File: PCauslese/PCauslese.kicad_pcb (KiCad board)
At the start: 2 copper layers, 78.7 x 24.1 mm, 29 parts, among them J1 Bally/Bergmann, J2 VDAI, J3 ADP alt, J4 ESP-01, J5 FT232, J7 USB TO TTL, J8 CP2102, U1 ULN2003A, U2 AMS1117-3.3, U4 MAX3232

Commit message: nochmal
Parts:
- added C8: C_Polarized, Capacitor_Tantalum_SMD:CP_EIA-3528-15_AVX-H, F.Cu at (119.7, 65.4)
- added C9: C_Polarized, Capacitor_Tantalum_SMD:CP_EIA-3528-15_AVX-H, F.Cu at (119.7, 69.2)
- added J6: Conn_01x08, Connector_PinHeader_2.54mm:PinHeader_1x08_P2.54mm_Vertical, F.Cu at (103.5, 66.0)
- added J9: Conn_01x08, Connector_PinHeader_2.54mm:PinHeader_1x08_P2.54mm_Vertical, F.Cu at (106.0, 66.0)
- added U3: AMS1117-5.0, Package_TO_SOT_SMD:SOT-223-3_TabPin2, F.Cu at (112.4, 69.0)
- moved J7 115.9 mm to (218.4, 46.4), turned to 0 degrees
- moved C7 109.4 mm to (194.9, 60.2)
- moved C1 105.7 mm to (178.4, 34.0), turned to 0 degrees
- moved J8 101.5 mm to (214.0, 43.2), turned to 0 degrees
- moved J5 100.0 mm to (209.4, 43.2), turned to 0 degrees
- moved U2 94.6 mm to (174.7, 22.2), turned to 0 degrees
- moved D1 92.9 mm to (206.5, 25.7)
- moved J4 92.2 mm to (194.9, 42.5), turned to 0 degrees
- moved R8 85.3 mm to (192.2, 36.2), turned to 0 degrees
- moved C2 85.1 mm to (178.4, 38.4), turned to 0 degrees
- moved C5 85.1 mm to (178.4, 51.4)
- moved C3 82.9 mm to (178.4, 42.7), turned to 0 degrees
- moved R9 82.8 mm to (188.4, 44.5)
- moved C4 79.0 mm to (178.4, 47.1), turned to 0 degrees
- moved U4 75.5 mm to (167.0, 43.8), turned to 0 degrees
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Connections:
- R2 pad 1: +3.3V -> VDDA
- R3 pad 1: +3.3V -> VDDA
- R4 pad 1: +3.3V -> VDDA
- R5 pad 1: +3.3V -> VDDA
- R7 pad 1: +3.3V -> VDDA
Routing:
- net +3.3V: track 86.1 -> 0.00 mm, vias 1 -> 0
- net GND: track 65.5 -> 6.99 mm, vias 13 -> 36
- net +48V: track 0.00 -> 48.3 mm
- net /DTR: track 44.1 -> 0.00 mm, vias 1 -> 0
- net BUSY: track 90.3 -> 48.3 mm, vias 1 -> 0
- net /RX: track 42.0 -> 0.00 mm
- net /TX: track 36.5 -> 0.00 mm
- net TX1: track 82.8 -> 52.7 mm
- net VDDA: track 0.00 -> 27.3 mm
- net Net-(D1-DIN): track 24.9 -> 0.00 mm
- net Net-(U1-I6): track 20.5 -> 0.00 mm
- net Net-(U4-VS+): track 14.6 -> 0.00 mm
- net RX1: track 94.8 -> 80.6 mm, vias 1 -> 0
- net Net-(JP1-A): track 17.2 -> 30.6 mm, vias 1 -> 0
- net Net-(U4-VS-): track 10.6 -> 0.00 mm
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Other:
- board text removed: "48V"
- board text removed: "BUSY"
- board text removed: "DTR"
- board text removed: "GND"
- board text removed: "MAX3232(3V) MAX232 (5V)"
- board text removed: "RX"
- board text removed: "SSA"
- board text removed: "SSE"
- board text removed: "TX"
- board text removed: "VPP"
- board text removed: "normal"

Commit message: max mit esp
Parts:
- added J10: Conn_01x05, Connector_PinHeader_2.54mm:PinHeader_1x05_P2.54mm_Vertical, F.Cu at (129.5, 69.8)
- added J11: Conn_01x05, Connector_PinHeader_2.54mm:PinHeader_1x05_P2.54mm_Vertical, F.Cu at (132.1, 69.8)
- U2: value AMS1117-3.3 -> 1117-3.3
- U3: value AMS1117-5.0 -> 1117-5.0
- moved D1 89.9 mm to (137.7, 83.6), turned to 180 degrees
- moved J7 69.9 mm to (160.7, 85.7), turned to 90 degrees
- moved U2 61.3 mm to (139.5, 72.4), turned to -90 degrees
- moved J8 53.7 mm to (165.7, 66.7)
- moved J5 53.5 mm to (161.3, 66.7)
- moved C1 53.5 mm to (135.5, 66.0), turned to 180 degrees
- moved R8 52.0 mm to (148.8, 64.8)
- moved C7 50.6 mm to (144.6, 66.0), turned to 180 degrees
- moved C3 48.2 mm to (153.7, 84.1), turned to 90 degrees
- moved J4 47.9 mm to (155.6, 69.8), turned to -90 degrees
- moved C2 46.8 mm to (140.7, 66.0)
- moved C6 43.4 mm to (147.1, 85.7), turned to 180 degrees
- moved R9 41.0 mm to (152.8, 64.8)
- moved C4 40.4 mm to (153.7, 79.0), turned to 90 degrees
- moved U4 40.1 mm to (147.4, 78.7), turned to 180 degrees
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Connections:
- C1 pad 1: VPP -> VDDA
- U2 pad 3: VPP -> VDDA
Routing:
- net +3.3V: track 0.00 -> 51.6 mm, vias 0 -> 3
- net /RX: track 0.00 -> 42.4 mm
- net Net-(J10-Pin_3): track 0.00 -> 39.5 mm, vias 0 -> 2
- net /TX: track 0.00 -> 38.8 mm
- net Net-(D1-DIN): track 0.00 -> 36.8 mm, vias 0 -> 1
- net VDDA: track 27.3 -> 62.7 mm, vias 0 -> 1
- net /DTR: track 0.00 -> 34.8 mm
- net Net-(J10-Pin_5): track 0.00 -> 27.7 mm
- net Net-(J10-Pin_1): track 0.00 -> 23.0 mm, vias 0 -> 1
- net GND: track 6.99 -> 12.9 mm, vias 36 -> 75
- net Net-(U4-VS+): track 0.00 -> 5.20 mm
- net Net-(U4-VS-): track 0.00 -> 5.09 mm
- net Net-(U4-C1+): track 0.00 -> 4.82 mm
- net Net-(U4-C1-): track 0.00 -> 4.60 mm
- net Net-(U4-C2+): track 0.00 -> 4.29 mm
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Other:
- board size 78.7 x 24.1 mm -> 97.2 x 24.1 mm
- board text added: "40V"
- board text added: "BUSY"
- board text added: "DTR"
- board text added: "GND"
- board text added: "JLCJLCJLCJLC"
- board text added: "RX"
- board text added: "RX1"
- board text added: "RX2"
- board text added: "Stecker"
- board text added: "TX"
- board text added: "TX1"
- board text added: "TX2"
- board text added: "VDD"
- board text added: "VPP"
- board text added: "Verstärker /Adapter"
- board text added: "https://github.com/stonedDiscord/Automatenplatinen"
- board text added: "normal"

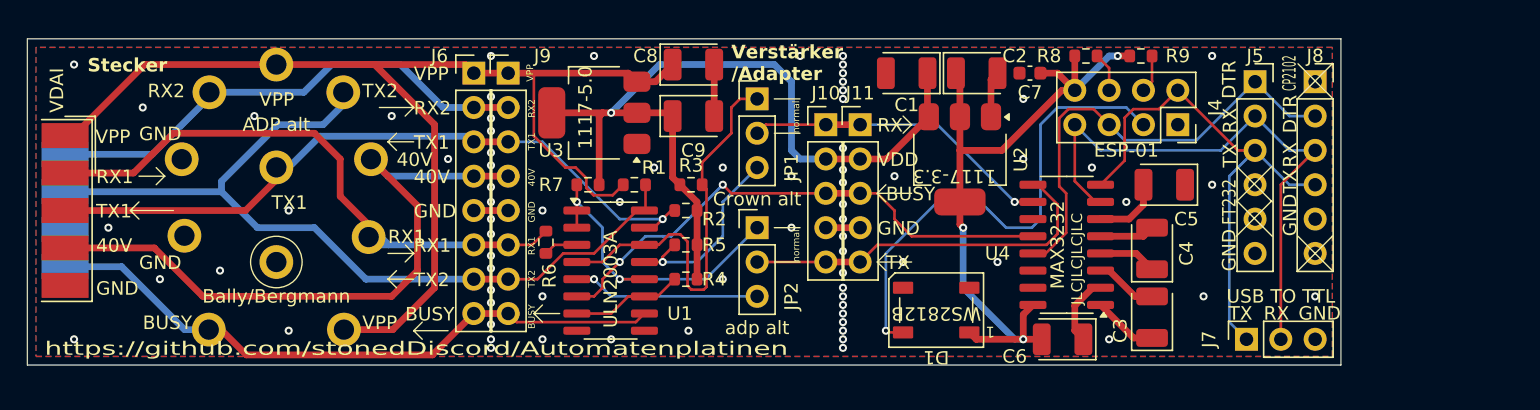
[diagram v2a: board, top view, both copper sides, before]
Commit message: wlan abbrech
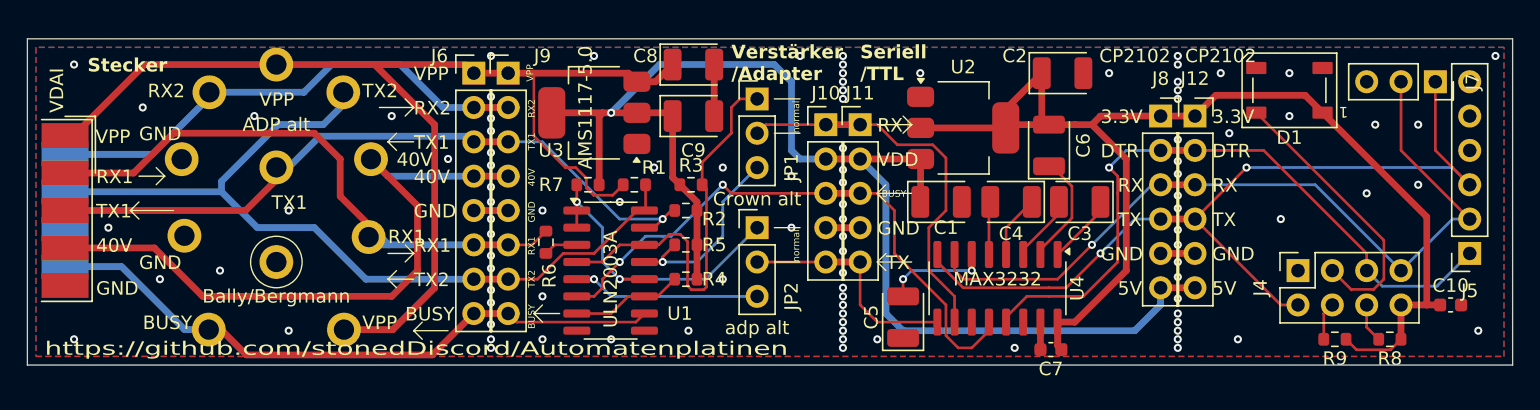
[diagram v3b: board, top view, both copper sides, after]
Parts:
- added C10: C, Capacitor_SMD:C_0603_1608Metric, F.Cu at (175.8, 83.2)
- added J12: CP2102, Connector_PinSocket_2.54mm:PinSocket_1x06_P2.54mm_Vertical, F.Cu at (156.8, 69.2)
- U2: value 1117-3.3 -> AMS1117-3.3
- U3: value 1117-5.0 -> AMS1117-5.0
- moved D1 30.8 mm to (163.8, 67.3)
- moved R8 30.7 mm to (171.3, 85.7), turned to 180 degrees
- moved R9 25.4 mm to (167.2, 85.7), turned to 180 degrees
- moved J7 23.6 mm to (174.6, 66.7), turned to -90 degrees
- moved C5 21.7 mm to (135.3, 84.1), turned to 90 degrees
- moved C7 20.5 mm to (146.2, 86.5)
- moved J5 20.3 mm to (177.2, 79.4), turned to 180 degrees
- moved C6 14.4 mm to (146.1, 71.4), turned to 90 degrees
- moved J4 14.0 mm to (164.5, 80.6), turned to 90 degrees
- moved J8 11.7 mm to (154.3, 69.2)
- moved C4 11.0 mm to (143.2, 75.6), turned to 180 degrees
- moved C3 10.1 mm to (148.3, 75.6), turned to 180 degrees
- moved C1 9.86 mm to (138.1, 75.6), turned to 0 degrees
- moved C2 6.35 mm to (147.1, 66.0)
- moved U4 6.05 mm to (142.2, 82.0), turned to -90 degrees
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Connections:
- J8 pad 6: +5V -> VDDA
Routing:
- net +3.3V: track 51.6 -> 88.7 mm, vias 3 -> 0
- net VDDA: track 62.7 -> 98.4 mm
- net /TX: track 38.8 -> 63.8 mm, vias 0 -> 2
- net /RX: track 42.4 -> 58.9 mm, vias 0 -> 1
- net /DTR: track 34.8 -> 50.7 mm, vias 0 -> 1
- net Net-(D1-DIN): track 36.8 -> 20.9 mm, vias 1 -> 0
- net Net-(J10-Pin_5): track 27.7 -> 17.0 mm
- net Net-(J10-Pin_1): track 23.0 -> 28.7 mm, vias 1 -> 0
- net Net-(J10-Pin_3): track 39.5 -> 43.6 mm
- net Net-(U4-VS+): track 5.20 -> 8.33 mm
- net Net-(U4-VS-): track 5.09 -> 7.80 mm, vias 0 -> 2
- net GND: track 12.9 -> 14.1 mm, vias 75 -> 99
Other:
- board size 97.2 x 24.1 mm -> 109.9 x 24.1 mm
- board text added: "3.3V"
- board text added: "5V"
- board text added: "Seriell /TTL"
- board text removed: "JLCJLCJLCJLC"

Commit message: auslese bestellt
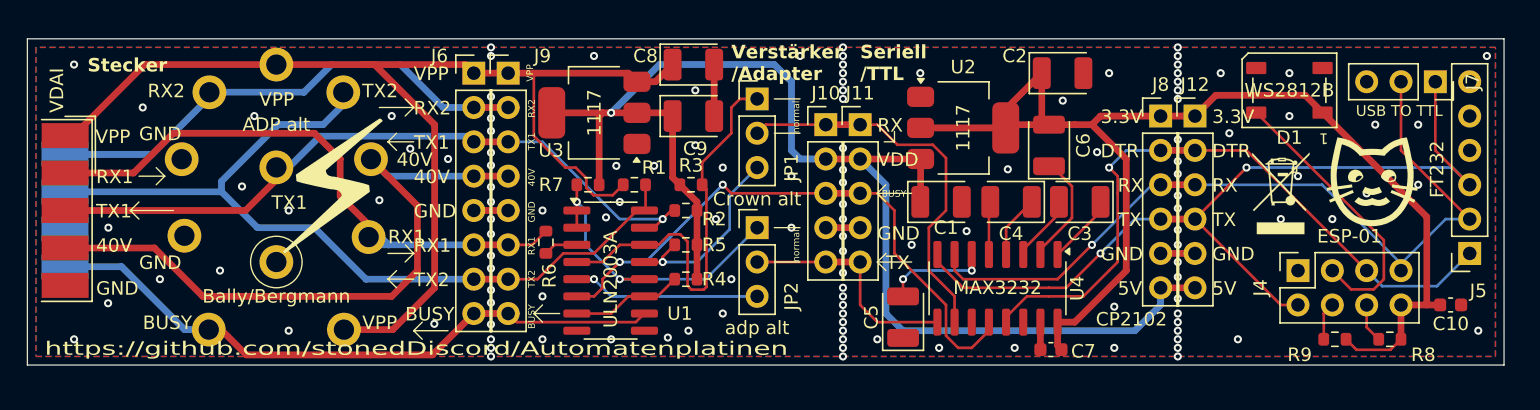
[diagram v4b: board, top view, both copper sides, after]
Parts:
- added REF**: WEEE-Logo_4.2x6mm_SilkScreen, Symbol:WEEE-Logo_4.2x6mm_SilkScreen, F.Cu at (163.2, 74.9)
- added Shikanoko Nokonoko Koshitantan: LOGO, LOGO, B.Cu at (145.8, 75.9)
- added 青山 剛昌: LOGO, LOGO, B.Cu at (103.3, 75.2)
- J12, J8: footprint Connector_PinSocket_2.54mm:PinSocket_1x06_P2.54mm_Vertical -> Connector_PinHeader_2.54mm:PinHeader_1x06_P2.54mm_Vertical
- U2: value AMS1117-3.3 -> 1117
- U3: value AMS1117-5.0 -> 1117
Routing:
- net /DTR: track 50.7 -> 49.9 mm
- net GND: vias 99 -> 128
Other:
- board size 109.9 x 24.1 mm -> 109.2 x 24.1 mm
- board text added: "⚡"
- board text added: "🐱"

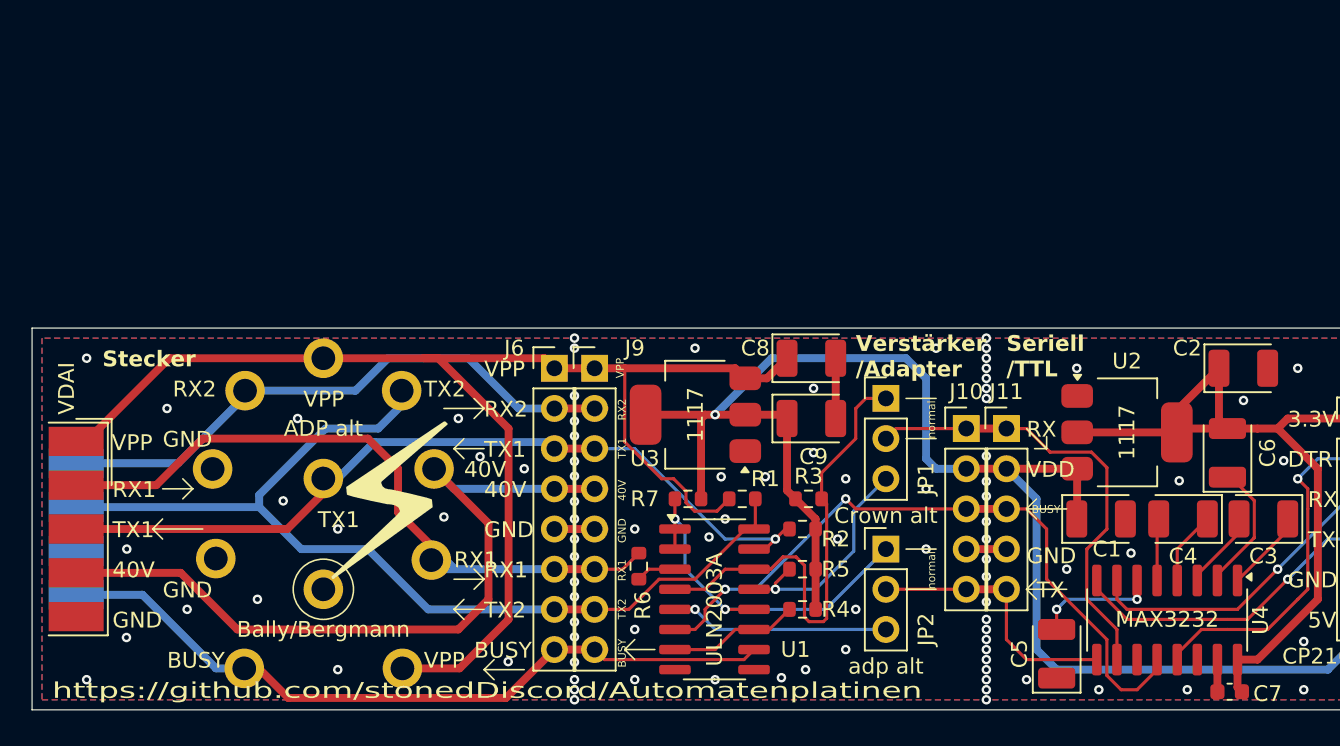
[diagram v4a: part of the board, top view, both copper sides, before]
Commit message: stecker korrigiert
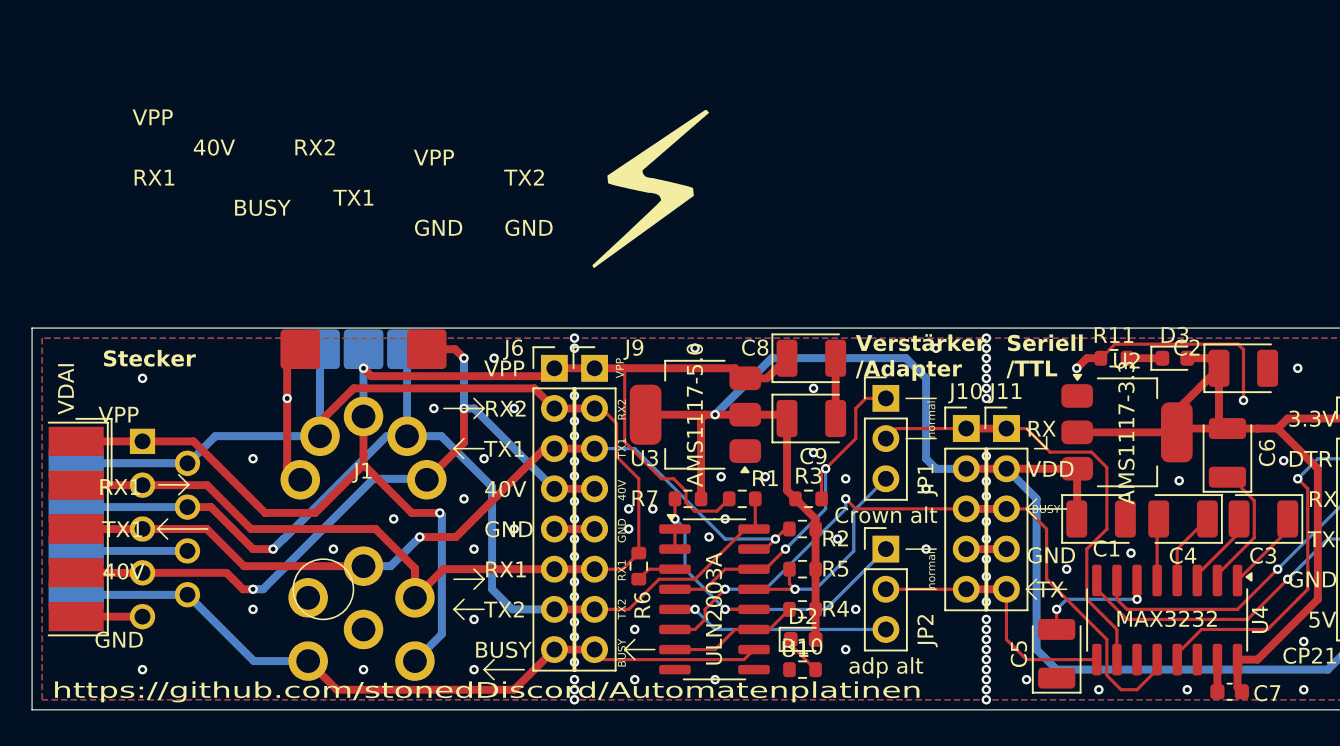
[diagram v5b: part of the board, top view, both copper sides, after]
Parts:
- removed 青山 剛昌: LOGO, LOGO
- added D2: LED, LED_SMD:LED_0603_1608Metric, F.Cu at (119.2, 83.2)
- added D3: LED, LED_SMD:LED_0603_1608Metric, F.Cu at (142.7, 65.4)
- added J13: ADP alt, DIN:DIN41524edge, B.Cu at (91.4, 64.8)
- added J14: VDAI, Connector_Dsub:DSUB-9_Male_Vertical_P2.77x2.84mm, B.Cu at (77.5, 70.7)
- added R10: 1k, Resistor_SMD:R_0603_1608Metric, F.Cu at (119.2, 85.1)
- added R11: 1k, Resistor_SMD:R_0603_1608Metric, F.Cu at (138.9, 65.4)
- U2: value 1117 -> AMS1117-3.3
- U3: value 1117 -> AMS1117-5.0
- moved J1 3.59 mm to (91.4, 82.5)
- moved J3 2.63 mm to (91.4, 73.1)
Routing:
- net GND: track 14.1 -> 41.1 mm, vias 128 -> 129
- net RX1: track 80.0 -> 92.6 mm
- net Net-(JP1-A): track 30.6 -> 22.9 mm, vias 0 -> 2
- net unconnected-(J14-Pad8): track 0.00 -> 7.04 mm
- net Net-(D2-K): track 0.00 -> 2.57 mm
- net +3.3V: track 88.7 -> 90.9 mm
- net Net-(D3-K): track 0.00 -> 2.24 mm
- net TX1: track 51.8 -> 54.0 mm, vias 1 -> 2
- net VDDA: track 98.4 -> 100.3 mm
- net TX2: track 63.0 -> 64.8 mm, vias 0 -> 1
- net +48V: track 48.7 -> 47.3 mm, vias 0 -> 3
- net VPP: track 88.3 -> 87.2 mm, vias 0 -> 2

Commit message: gnd
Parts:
- removed Shikanoko Nokonoko Koshitantan: LOGO, LOGO
- U2: value AMS1117-3.3 -> AMS1117
- U3: value AMS1117-5.0 -> AMS1117
- moved J2 3.18 mm to (76.5, 76.2)
- moved J14 1.78 mm to (79.2, 70.7)
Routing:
- net GND: track 41.1 -> 355.9 mm, vias 129 -> 130
- net Net-(J10-Pin_5): track 17.0 -> 24.2 mm
- net RX1: track 92.6 -> 86.3 mm
- net TX2: track 64.8 -> 61.6 mm
- net VPP: track 87.2 -> 84.1 mm
- net TX1: track 54.0 -> 50.8 mm
- net BUSY: track 46.9 -> 43.7 mm
- net +48V: track 47.3 -> 45.5 mm
- net unconnected-(J14-Pad8): track 7.04 -> 5.63 mm
- net VDDA: track 100.3 -> 99.3 mm, vias 1 -> 2
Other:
- board size 109.2 x 24.1 mm -> 105.2 x 24.1 mm

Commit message: werte
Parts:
- C3, C4, C5, C6: value C_Polarized -> 0.1 μF
- U2: value AMS1117 -> AMS1117-3.3
- U3: value AMS1117 -> AMS1117-5.0
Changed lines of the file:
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@@
 		(fp_arc
 			(start -1.5 6.5)
-			(mid 0 -6.670832)
+			(mid 0.000001 -6.670832)
 			(end 1.500001 6.5)
 			(stroke
@@
 			)
 		)
-		(property "Value" "C_Polarized"
+		(property "Value" "0.1 μF"
 			(at 0 2.35 90)
 			(layer "F.Fab")
@@
 			)
 		)
-		(property "Value" "C_Polarized"
+		(property "Value" "0.1 μF"
 			(at 0 2.35 90)
 			(layer "F.Fab")
@@
 			)
 		)
-		(property "Value" "C_Polarized"
+		(property "Value" "0.1 μF"
 			(at 0 2.35 0)
 			(layer "F.Fab")
@@
 			)
 		)
-		(property "Value" "C_Polarized"
+		(property "Value" "0.1 μF"
 			(at 0 2.35 0)
 			(layer "F.Fab")
@@
 			)
 		)
-		(property "Value" "AMS1117"
+		(property "Value" "AMS1117-5.0"
 			(at -1.245 0 90)
 			(layer "F.SilkS")
@@
 			)
 		)
-		(property "Value" "AMS1117"
+		(property "Value" "AMS1117-3.3"
 			(at 1.27 0 90)
 			(layer "F.SilkS")
@@
 		(fp_arc
 			(start 1.500001 -6.5)
-			(mid 0 6.670832)
+			(mid 0.000001 6.670832)
 			(end -1.5 -6.5)
 			(stroke
@@
 		(fp_arc
 			(start 10.883927 -5.57)
-			(mid 11.912386 -5.195671)
+			(mid 11.912389 -5.195672)
 			(end 12.459619 -4.247837)
 			(stroke

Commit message: cap werte
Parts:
- added R12: 10k, Resistor_SMD:R_0603_1608Metric, F.Cu at (159.4, 70.9)
- added R13: 10k, Resistor_SMD:R_0603_1608Metric, F.Cu at (159.5, 67.8)
- C1, C8: value C_Polarized -> 10uF
- C2, C9: value C_Polarized -> 22uF
- J14: footprint Connector_Dsub:DSUB-9_Male_Vertical_P2.77x2.84mm -> Connector_Dsub:DSUB-9_Pins_Vertical_P2.77x2.84mm
- J2: footprint Connector_Dsub:DSUB-9_Male_EdgeMount_P2.77mm -> Connector_Dsub:DSUB-9_Pins_EdgeMount_P2.77mm
- U2: value AMS1117-3.3 -> 1117-3.3
- U3: value AMS1117-5.0 -> 1117-5.0
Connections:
- net Net-(D1-DIN) renamed /GPIO2
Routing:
- net GND: track 355.9 -> 368.7 mm
- net +3.3V: track 90.9 -> 94.6 mm
- net /GPIO2: track 20.9 -> 23.0 mm
